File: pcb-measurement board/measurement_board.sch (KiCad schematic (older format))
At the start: 92 parts, among them P1 HDR DUAL ROW, P2 CONN_02X15, P3 CONN_02X13, P4 CONN_02X05, P5 CONN_02X05, Q1 Si1101X, U1 NX3L4051, U10 TLV1G125, U11 NX3L4051, U12 MSP430G2955, U13 AD8603, U14 TLV1G125, U15 MCP4921, U16 AD8293, U17 NX3L4051, U18 NX3L4051, U19 QS4A110, U2 TPS73133, U20 QS4A110, U21 TLV1G125, U22 TLV1G125, U3 74CBTLV3253, U4 NX3L4051, U5 TPS73125, U6 AD8603, U7 MCP4921, U8 NX3L4051, U9 TLV1G125

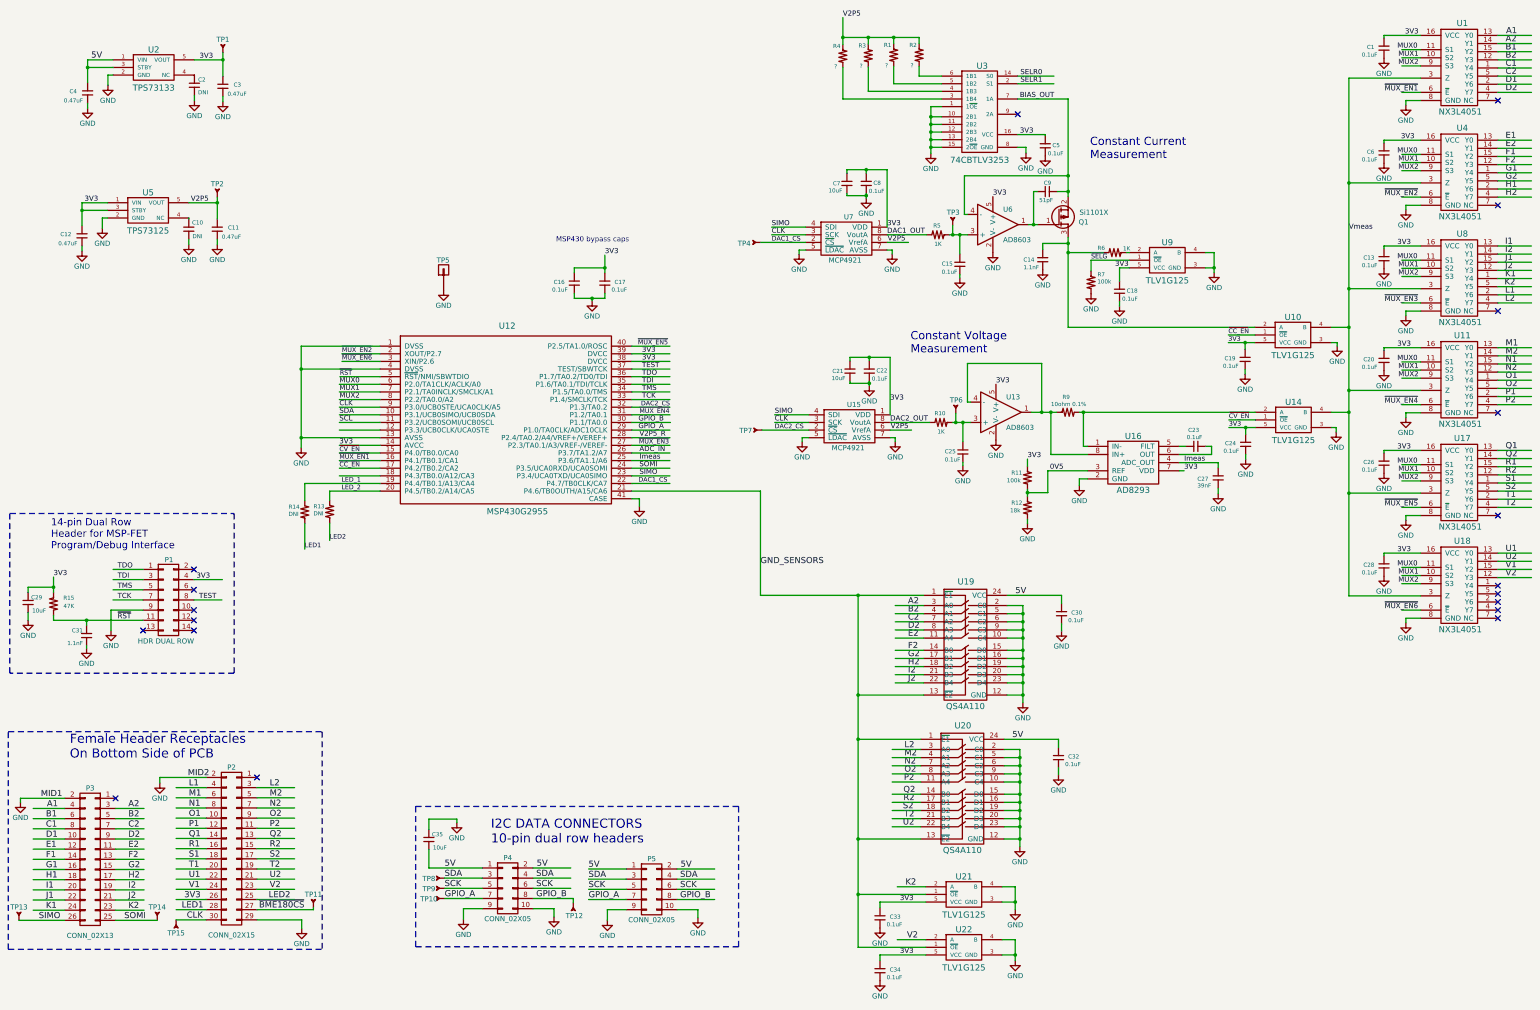
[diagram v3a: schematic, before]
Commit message: -more progress on the measurement board layout
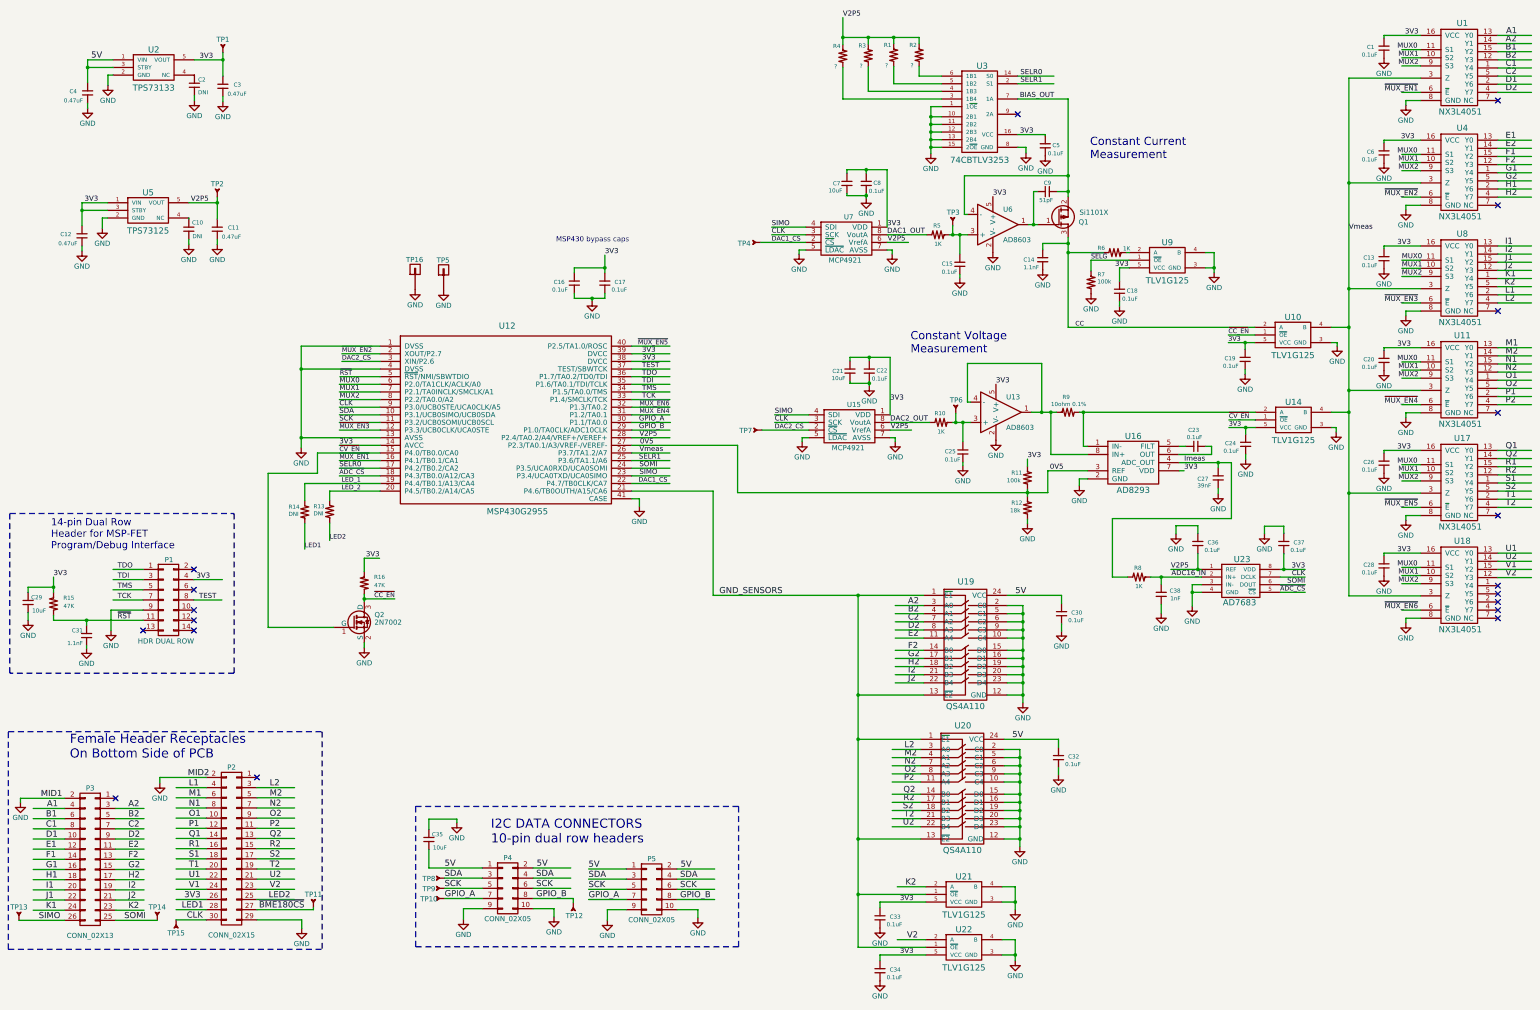
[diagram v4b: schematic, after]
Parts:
- added C36, C37: 0.1uF, footprints_on_Cdrive:0603, symbol CAP_NP
- added C38: 1nF, footprints_on_Cdrive:0603, symbol CAP_NP
- added Q2: 2N7002, footprints_on_Cdrive:SOT23, symbol 2N7002
- added R16: 47K, footprints_on_Cdrive:0603, symbol Res1_1
- added R8: 1K, footprints_on_Cdrive:0603, symbol Res1_1
- added TP16: header_pin, footprints_on_Cdrive:Header_Pin_Rnd, symbol header_pin
- added U23: AD7683, footprints_on_Cdrive:RM-8, symbol AD7683
- P4: description (none) -> CONN HEADER VERT 10POS .100 15AU; manufacturer (none) -> TE Connectivity; manufacturer pn (none) -> 5499922-1; supplier (none) -> digikey; supplier pn (none) -> AHK10H-ND
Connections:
- net labels added: ADC16_IN, CC, ~ADC_CS
- net labels removed: ADC_IN, SCL, V2P5_R
- wire segments 476 -> 509

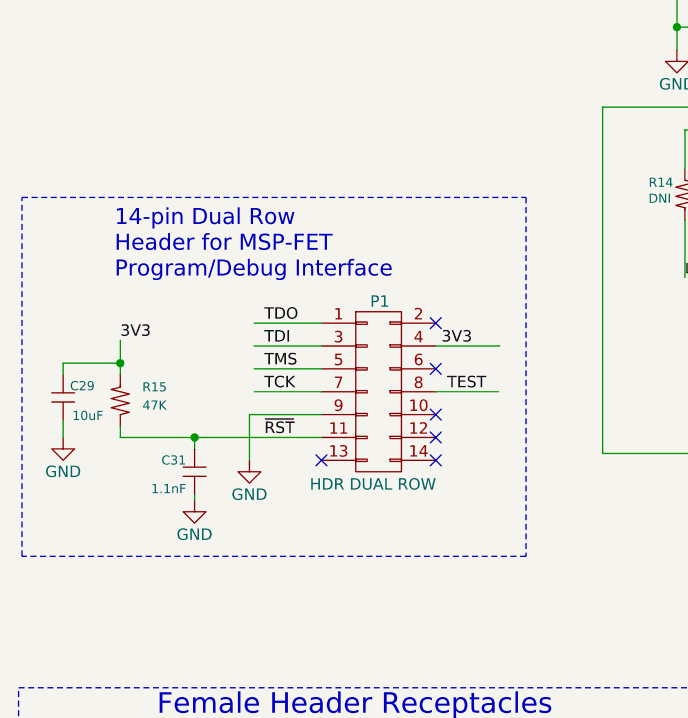
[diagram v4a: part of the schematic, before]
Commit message: -nearing completion of measurement board layout -routed most signal traces, just need to add testpoints and fix DRC voilations -changed MSP430 programming connector from 2x7 header to 10-pin flex cable connector
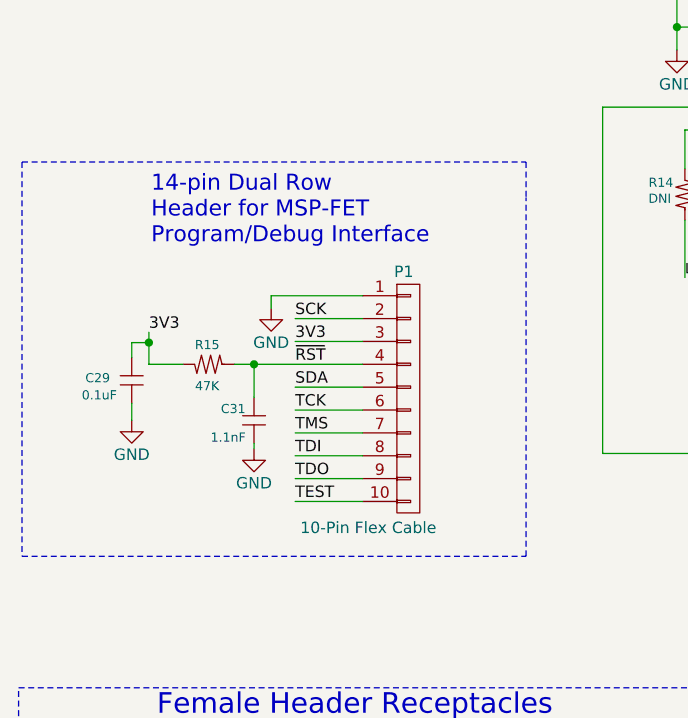
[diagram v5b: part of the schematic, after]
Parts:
- removed P1: HDR DUAL ROW, Pin_Headers:Pin_Header_Straight_2x07_Pitch2.54mm, symbol CONN_02X07
- added P1: 10-Pin Flex Cable, footprints_on_Cdrive:WM6745-FPC, symbol CONN_01X10
- C29: value 10uF -> 0.1uF; description CAP CER 10UF 6.3V X5R 0603 -> CAP CER 0.1UF 16V X7R 0603; manufacturer Murata -> AVX Corporation; manufacturer pn GRM188R60J106ME47D -> GRM188R71C104KA01D; supplier pn 490-3896-1-ND -> 490-1532-1-ND
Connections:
- wire segments 509 -> 511
- no-connect marks 19 -> 13
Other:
- moved on the sheet: C31, R15

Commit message: -layout of measurement board completed -gerber files created -added a pdf of the schematic
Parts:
- removed TP11, TP13, TP14, TP15, TP6, TP7: TP_SMT, footprints_on_Cdrive:TP_SMT.02, symbol TP_SMT
- added C39: 10pF, footprints_on_Cdrive:0402, symbol CAP_NP
- added C40: 0.1uF, footprints_on_Cdrive:0603, symbol CAP_NP
- added R17: 0 ohm, footprints_on_Cdrive:0402, symbol Res1_1
- added R18: DNI, footprints_on_Cdrive:0402, symbol Res1_1
- P4, P5: footprint Pin_Headers:Pin_Header_Straight_2x05_Pitch2.54mm -> footprints_on_Cdrive:header_2x5_idc
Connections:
- wire segments 511 -> 516
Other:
- moved on the sheet: R12

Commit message: -added BOM and files for measurement board assembly house
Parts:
- C38: value 1nF -> 1.1nF; description CAP CER 1000PF 16V X7R 0603 -> CAP CER 1100PF 50V C0G/NP0 0603; manufacturer Kemet -> Murata; manufacturer pn C0603C102K4RACTU -> GRM1885C1H112JA01D; supplier pn 399-7835-1-ND -> 490-1452-1-ND
- P1: value 10-Pin Flex Cable -> 10-Pin Flex Conn
- P2: description CONN HEADER B/A 30POS VERT DUAL SMT -> CONN RECEPT 30POS .100 VERT DUAL; manufacturer pn 2-146134-1 -> 1-534998-5; supplier pn A107235-ND -> A26494-ND
- P3: description CONN RECEPT 30POS .100 VERT DUAL -> CONN RECEPT 26POS .100 VERT DUAL; manufacturer pn 1-534998-5 -> 1-534998-3; supplier pn A26494-ND -> A26492-ND
- P4: description CONN HEADER VERT 10POS .100 15AU -> CONN HEADER .100\" DUAL STR 80POS; manufacturer TE Connectivity -> Sullins Connector; manufacturer pn 5499922-1 -> PREC040DAAN-RC; supplier pn AHK10H-ND -> S2012EC-40-ND
- Q1: value Si1101X -> Si1103X; description MOSFET P-CH 12V SC-89 -> MOSFET P-CH 20V 350MA SC89-3; manufacturer pn SI1011X-T1-GE3 -> SI1013X-T1-GE3; supplier pn SI1011X-T1-GE3CT-ND -> SI1013X-T1-GE3CT-ND
- R1: value ? -> 30k; description (none) -> RES SMD 30K OHM 1% 1/10W 0603; manufacturer pn (none) -> RC0603FR-0730KL; supplier pn (none) -> 311-30.0KHRCT-ND
- R12: value 18k -> 24.9k; description RES SMD 18K OHM 1% 1/10W 0603 -> RES SMD 24.9K OHM 1% 1/10W 0603; manufacturer pn RC0603FR-0718KL -> RC0603FR-0724K9L; supplier pn 311-18.0KHRCT-ND -> 311-24.9KHRCT-ND
- R2: value ? -> 75k; description (none) -> RES SMD 75K OHM 1% 1/10W 0603; manufacturer pn (none) -> RC0603FR-0775KL; supplier pn (none) -> 311-75.0KHRCT-ND
- R3: value ? -> 10k; description (none) -> RES SMD 10K OHM 1% 1/10W 0603; manufacturer pn (none) -> RC0603FR-0710KL; supplier pn (none) -> 311-10.0KHRCT-ND
- R4: value ? -> 2k; description (none) -> RES SMD 2K OHM 1% 1/10W 0603; manufacturer pn (none) -> RC0603FR-072KL; supplier pn (none) -> 311-2.00KHRCT-ND
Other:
- note added: "Flat Flex Cable Connector for\nMSP-FET Program/Debug Interface"
- note removed: "14-pin Dual Row\nHeader for MSP-FET\nProgram/Debug Interface"
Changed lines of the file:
@@
 Sheet 1 1
 Title "Schematic - NEA Sensor Measurement PCB"
-Date "2017-05-08"
+Date "2017-05-12"
 Rev "1"
-Comp "Custom Silicon Solutions"
+Comp "Custom Silicon Solutions, Inc."
 Comment1 ""
 Comment2 ""
@@
 Text Label 11570 3215 0    45   ~ 0
 ~SELG
-$Comp
-L Res1_1 R4
-U 1 1 574226CA
-P 9130 1220
-F 0 "R4" H 9190 1110 40  0000 C CNN
-F 1 "?" H 9200 1310 40  0000 C CNN
-F 2 "footprints_on_Cdrive:0603" H 9185 940 30  0001 C CNN
-F 3 "" H 9130 1220 30  0000 C CNN
-F 4 " " H 9480 850 60  0001 C CNN "description"
-F 5 "digikey" H 8920 735 60  0001 C CNN "supplier"
-F 6 " " H 9725 720 60  0001 C CNN "supplier pn"
-F 7 "Yageo" H 8505 610 60  0001 C CNN "manufacturer"
-F 8 " " H 9605 615 60  0001 C CNN "manufacturer pn"
-	1    9130 1220
-	-1   0    0    1
-$EndComp
 Text Label 4180 4810 0    50   ~ 0
 SCK
@@
 P 11245 2790
 F 0 "Q1" H 11545 2840 50  0000 R CNN
-F 1 "Si1101X" H 11740 2745 50  0000 R CNN
+F 1 "Si1103X" H 11740 2745 50  0000 R CNN
 F 2 "footprints_on_Cdrive:SOT23" H 11445 2890 50  0001 C CNN
 F 3 "" H 11245 2790 50  0000 C CNN
-F 4 "SI1011X-T1-GE3CT-ND " H 11720 3190 50  0001 C CNN "supplier pn"
+F 4 "SI1013X-T1-GE3CT-ND " H 11720 3190 50  0001 C CNN "supplier pn"
 F 5 "digikey" H 11070 3190 50  0001 C CNN "supplier"
 F 6 "Vishay" H 11095 3290 50  0001 C CNN "manufacturer"
-F 7 "SI1011X-T1-GE3 " H 11595 3290 50  0001 C CNN "manufacturer pn"
-F 8 "MOSFET P-CH 12V SC-89 " H 11445 3490 50  0001 C CNN "description"
+F 7 "SI1013X-T1-GE3 " H 11595 3290 50  0001 C CNN "manufacturer pn"
+F 8 "MOSFET P-CH 20V 350MA SC89-3 " H 11445 3490 50  0001 C CNN "description"
 	1    11245 2790
 	1    0    0    1
@@
 	1    0    0    -1
 $EndComp
-Text Label 9565 2890 0    50   ~ 0
+Text Label 9565 2720 0    50   ~ 0
 3V3
 $Comp
@@
 F 3 "" H 3120 7850 50  0000 C CNN
 F 4 "digikey" H 3120 9000 60  0001 C CNN "supplier"
-F 5 "A107235-ND " H 3120 9000 60  0001 C CNN "supplier pn"
+F 5 "A26494-ND" H 3120 9000 60  0001 C CNN "supplier pn"
 F 6 "TE" H 3120 9000 60  0001 C CNN "manufacturer"
-F 7 "2-146134-1 " H 3120 9000 60  0001 C CNN "manufacturer pn"
-F 8 "CONN HEADER B/A 30POS VERT DUAL SMT" H 3120 9000 60  0001 C CNN "description"
+F 7 "1-534998-5" H 3120 9000 60  0001 C CNN "manufacturer pn"
+F 8 " CONN RECEPT 30POS .100 VERT DUAL " H 3120 9000 60  0001 C CNN "description"
 	1    3120 9000
 	-1   0    0    -1
@@
 F 3 "" H 1730 7955 50  0000 C CNN
 F 4 "digikey" H 1730 9105 60  0001 C CNN "supplier"
-F 5 "A26494-ND" H 1730 9105 60  0001 C CNN "supplier pn"
+F 5 "A26492-ND" H 1730 9105 60  0001 C CNN "supplier pn"
 F 6 "TE" H 1730 9105 60  0001 C CNN "manufacturer"
-F 7 "1-534998-5 " H 1730 9105 60  0001 C CNN "manufacturer pn"
-F 8 "CONN RECEPT 30POS .100 VERT DUAL " H 1730 9105 60  0001 C CNN "description"
+F 7 "1-534998-3" H 1730 9105 60  0001 C CNN "manufacturer pn"
+F 8 "CONN RECEPT 26POS .100 VERT DUAL " H 1730 9105 60  0001 C CNN "description"
 	1    1730 9105
 	-1   0    0    -1
@@
 Text Label 4180 4585 0    50   ~ 0
 MUX2
-Text Notes 1505 5915 0    70   ~ 0
-14-pin Dual Row\nHeader for MSP-FET\nProgram/Debug Interface
+Text Notes 1115 5870 0    70   ~ 0
+Flat Flex Cable Connector for\nMSP-FET Program/Debug Interface
 $Comp
 L CAP_NP C31
@@
 F 3 "" H 5835 8190 50  0000 C CNN
 F 4 "digikey" H 5835 9390 60  0001 C CNN "supplier"
-F 5 " AHK10H-ND" H 5835 9390 60  0001 C CNN "supplier pn"
-F 6 "TE Connectivity" H 5835 9390 60  0001 C CNN "manufacturer"
-F 7 " 5499922-1 " H 5835 9390 60  0001 C CNN "manufacturer pn"
-F 8 "CONN HEADER VERT 10POS .100 15AU " H 5835 9390 60  0001 C CNN "description"
+F 5 " S2012EC-40-ND " H 5835 9390 60  0001 C CNN "supplier pn"
+F 6 "Sullins Connector" H 5835 9390 60  0001 C CNN "manufacturer"
+F 7 " PREC040DAAN-RC " H 5835 9390 60  0001 C CNN "manufacturer pn"
+F 8 "CONN HEADER .100\" DUAL STR 80POS " H 5835 9390 60  0001 C CNN "description"
 	1    5835 9390
 	1    0    0    -1
@@
 P 10945 5740
 F 0 "R12" H 11050 5680 40  0000 C CNN
-F 1 "18k" H 11065 5755 40  0000 C CNN
+F 1 "24.9k" H 11085 5755 40  0000 C CNN
 F 2 "footprints_on_Cdrive:0603" H 11000 5460 30  0001 C CNN
 F 3 "" H 10945 5740 30  0000 C CNN
-F 4 " RES SMD 18K OHM 1% 1/10W 0603 " H 11295 5370 60  0001 C CNN "description"
+F 4 "RES SMD 24.9K OHM 1% 1/10W 0603 " H 11295 5370 60  0001 C CNN "description"
 F 5 "digikey" H 10735 5255 60  0001 C CNN "supplier"
-F 6 " 311-18.0KHRCT-ND " H 11540 5240 60  0001 C CNN "supplier pn"
+F 6 "311-24.9KHRCT-ND " H 11540 5240 60  0001 C CNN "supplier pn"
 F 7 "Yageo" H 10320 5130 60  0001 C CNN "manufacturer"
-F 8 "RC0603FR-0718KL " H 11420 5135 60  0001 C CNN "manufacturer pn"
+F 8 "RC0603FR-0724K9L " H 11420 5135 60  0001 C CNN "manufacturer pn"
 	1    10945 5740
 	-1   0    0    1
@@
 P 9380 1215
 F 0 "R3" H 9440 1105 40  0000 C CNN
-F 1 "?" H 9450 1305 40  0000 C CNN
+F 1 "10k" H 9485 1310 40  0000 C CNN
 F 2 "footprints_on_Cdrive:0603" H 9435 935 30  0001 C CNN
 F 3 "" H 9380 1215 30  0000 C CNN
-F 4 " " H 9730 845 60  0001 C CNN "description"
+F 4 "RES SMD 10K OHM 1% 1/10W 0603 " H 9730 845 60  0001 C CNN "description"
 F 5 "digikey" H 9170 730 60  0001 C CNN "supplier"
-F 6 " " H 9975 715 60  0001 C CNN "supplier pn"
+F 6 "311-10.0KHRCT-ND " H 9975 715 60  0001 C CNN "supplier pn"
 F 7 "Yageo" H 8755 605 60  0001 C CNN "manufacturer"
-F 8 " " H 9855 610 60  0001 C CNN "manufacturer pn"
+F 8 "RC0603FR-0710KL " H 9855 610 60  0001 C CNN "manufacturer pn"
 	1    9380 1215
 	-1   0    0    1
@@
 P 9630 1210
 F 0 "R1" H 9690 1100 40  0000 C CNN
-F 1 "?" H 9700 1300 40  0000 C CNN
+F 1 "30k" H 9725 1310 40  0000 C CNN
 F 2 "footprints_on_Cdrive:0603" H 9685 930 30  0001 C CNN
 F 3 "" H 9630 1210 30  0000 C CNN
-F 4 " " H 9980 840 60  0001 C CNN "description"
+F 4 "RES SMD 30K OHM 1% 1/10W 0603 " H 9980 840 60  0001 C CNN "description"
 F 5 "digikey" H 9420 725 60  0001 C CNN "supplier"
-F 6 " " H 10225 710 60  0001 C CNN "supplier pn"
+F 6 "311-30.0KHRCT-ND " H 10225 710 60  0001 C CNN "supplier pn"
 F 7 "Yageo" H 9005 600 60  0001 C CNN "manufacturer"
-F 8 " " H 10105 605 60  0001 C CNN "manufacturer pn"
+F 8 "RC0603FR-0730KL " H 10105 605 60  0001 C CNN "manufacturer pn"
 	1    9630 1210
 	-1   0    0    1
@@
 P 9880 1210
 F 0 "R2" H 9940 1100 40  0000 C CNN
-F 1 "?" H 9950 1300 40  0000 C CNN
+F 1 "75k" H 9950 1300 40  0000 C CNN
 F 2 "footprints_on_Cdrive:0603" H 9935 930 30  0001 C CNN
 F 3 "" H 9880 1210 30  0000 C CNN
-F 4 " " H 10230 840 60  0001 C CNN "description"
+F 4 "RES SMD 75K OHM 1% 1/10W 0603 " H 10230 840 60  0001 C CNN "description"
 F 5 "digikey" H 9670 725 60  0001 C CNN "supplier"
-F 6 " " H 10475 710 60  0001 C CNN "supplier pn"
+F 6 "311-75.0KHRCT-ND " H 10475 710 60  0001 C CNN "supplier pn"
 F 7 "Yageo" H 9255 600 60  0001 C CNN "manufacturer"
-F 8 " " H 10355 605 60  0001 C CNN "manufacturer pn"
+F 8 "RC0603FR-0775KL " H 10355 605 60  0001 C CNN "manufacturer pn"
 	1    9880 1210
 	-1   0    0    1
@@
 	0    -1   -1   0
 $EndComp
-$Comp
-L CAP_NP C38
-U 1 1 591216F7
-P 12260 6550
-F 0 "C38" H 12070 6635 40  0000 L CNN
-F 1 "1nF" H 12070 6560 40  0000 L CNN
-F 2 "footprints_on_Cdrive:0603" H 12298 6400 30  0001 C CNN
-F 3 "" H 12260 6550 60  0000 C CNN
-F 4 "CAP CER 1000PF 16V X7R 0603" H 12260 6550 60  0001 C CNN "description"
-F 5 "digikey" H 12260 6550 60  0001 C CNN "supplier"
-F 6 " 399-7835-1-ND " H 12260 6550 60  0001 C CNN "supplier pn"
-F 7 "Kemet" H 12260 6550 60  0001 C CNN "manufacturer"
-F 8 "C0603C102K4RACTU " H 12260 6550 60  0001 C CNN "manufacturer pn"
-	1    12260 6550
-	-1   0    0    -1
-$EndComp
 Text Label 11415 3875 0    45   ~ 0
 CC
@@
 P 2630 6585
 F 0 "P1" H 2610 7140 50  0000 C CNN
-F 1 "10-Pin Flex Cable" H 2455 6020 50  0000 C CNN
+F 1 "10-Pin Flex Conn" H 2455 6020 50  0000 C CNN
 F 2 "footprints_on_Cdrive:WM6745-FPC" H 2555 5810 60  0001 C CNN
 F 3 "" H 2630 6585 60  0000 C CNN
@@
 	-1   0    0    -1
 $EndComp
+$Comp
+L CAP_NP C38
+U 1 1 591C409B
+P 12260 6550
+F 0 "C38" H 12070 6600 40  0000 L CNN
+F 1 "1.1nF" H 12070 6525 40  0000 L CNN
+F 2 "footprints_on_Cdrive:0603" H 12298 6400 30  0001 C CNN
+F 3 "" H 12260 6550 60  0000 C CNN
+F 4 " CAP CER 1100PF 50V C0G/NP0 0603 " H 12260 6550 60  0001 C CNN "description"
+F 5 "digikey" H 12260 6550 60  0001 C CNN "supplier"
+F 6 " 490-1452-1-ND " H 12260 6550 60  0001 C CNN "supplier pn"
+F 7 "Murata" H 12260 6550 60  0001 C CNN "manufacturer"
+F 8 "GRM1885C1H112JA01D " H 12260 6550 60  0001 C CNN "manufacturer pn"
+	1    12260 6550
+	-1   0    0    -1
+$EndComp
+Connection ~ 12410 7110
+$Comp
+L Res1_1 R4
+U 1 1 5916886A
+P 9130 1195
+F 0 "R4" H 9055 1275 40  0000 C CNN
+F 1 "2k" H 9040 1075 40  0000 C CNN
+F 2 "footprints_on_Cdrive:0603" H 9185 915 30  0001 C CNN
+F 3 "" H 9130 1195 30  0000 C CNN
+F 4 " RES SMD 2K OHM 1% 1/10W 0603 " H 9480 825 60  0001 C CNN "description"
+F 5 "digikey" H 8920 710 60  0001 C CNN "supplier"
+F 6 " 311-2.00KHRCT-ND " H 9725 695 60  0001 C CNN "supplier pn"
+F 7 "Yageo" H 8505 585 60  0001 C CNN "manufacturer"
+F 8 " RC0603FR-072KL " H 9605 590 60  0001 C CNN "manufacturer pn"
+	1    9130 1195
+	1    0    0    -1
+$EndComp
 $EndSCHEMATC
